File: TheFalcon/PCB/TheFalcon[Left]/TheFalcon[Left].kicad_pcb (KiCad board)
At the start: 2 copper layers, 173.3 x 142.5 mm, 171 parts, among them IC1 IS31FL3729-QFLS4-TR, J2 Conn_01x04_Pin, J3 Conn_01x04_Pin, J5 Conn_01x01, J6 Conn_01x01, SW1 SW_Push, SW2 SW_Push, U2 USBLC6-2P6, U3 USBLC6-2P6, U4 AMS1117-3.3, U6 STM32G431CBTx, Y1 X322516MOB4SI

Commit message: Save
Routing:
- net /RGB Array/R_RGB_ROW_2: track 143.3 -> 133.7 mm, vias 12 -> 0
- net /RGB Array/R_RGB_ROW_1: track 143.6 -> 134.4 mm, vias 12 -> 0
- net /RGB Array/R_RGB_ROW_0: track 148.1 -> 139.5 mm, vias 12 -> 0
- net /RGB Array/R_RGB_ROW_4: track 124.9 -> 117.0 mm, vias 10 -> 0
- net /RGB Array/R_RGB_ROW_3: track 140.8 -> 133.1 mm, vias 10 -> 0
- net +5V: track 141.1 -> 138.5 mm, vias 2 -> 0
- net /RGB Array/G_RGB_ROW_3: track 152.0 -> 150.5 mm, vias 2 -> 0
- added copper zone on In2.Cu, net GND
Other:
- copper layers 2 -> 4

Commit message: Save
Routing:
- net /RGB Array/G_RGB_ROW_0: track 162.3 -> 0.00 mm
- net /RGB Array/G_RGB_ROW_1: track 159.8 -> 1.56 mm
- net Row3: track 152.5 -> 0.00 mm
- net /RGB Array/B_RGB_ROW_2: track 152.2 -> 0.00 mm
- net /RGB Array/G_RGB_ROW_2: track 156.1 -> 6.92 mm
- net /RGB Array/B_RGB_ROW_1: track 148.9 -> 0.00 mm
- net /RGB Array/B_RGB_ROW_0: track 148.2 -> 0.00 mm
- net /RGB Array/B_RGB_ROW_3: track 145.5 -> 0.00 mm
- net Row1: track 136.7 -> 0.00 mm
- net Row2: track 136.4 -> 0.00 mm
- net /RGB Array/G_RGB_ROW_3: track 150.5 -> 15.6 mm
- net Row0: track 130.3 -> 0.00 mm
- net /RGB Array/G_RGB_ROW_4: track 133.3 -> 5.19 mm
- net /RGB Array/B_RGB_ROW_4: track 127.8 -> 0.00 mm
- net /RGB Array/R_RGB_ROW_3: track 133.1 -> 6.27 mm
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- added copper zone on In1.Cu, net GND
- removed copper zone on F.Cu, net GND

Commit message: Save
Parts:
- S1, S10, S11, S12, S13, S14, S15, S16, S17, S18, S19, S2, S20, S21, S22, S23, S24, S25, S26, S27, S28, S29, S3, S30, S31, S32, S33, S34, S4, S5, S6, S7, S8, S9: footprint Gateron_KS33_Hotswap:Gateron-KS33-Hotswap-1U_Model -> MX_KS33:MX_KS33-Solderable-1U; moved to F.Cu
- S35, S36: footprint Gateron_KS33_Hotswap:Gateron-KS33-Hotswap-1.5U -> MX_KS33:MX_KS33-Solderable-1.5U; moved to F.Cu

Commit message: Save
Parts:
- moved C9 129.4 mm to (129.5, 20.9), turned to 0 degrees
- moved SW1 128.6 mm to (133.9, 20.7), turned to 180 degrees
- moved R24 114.2 mm to (99.3, 129.1)
- moved R33 114.0 mm to (97.5, 127.1)
- moved C12 110.7 mm to (85.6, 126.1)
- moved IC1 110.7 mm to (84.0, 129.3)
- moved C13 110.7 mm to (85.6, 124.6)
- moved R6 110.7 mm to (87.6, 126.8)
- moved R4 109.8 mm to (150.4, 21.1)
- moved SW2 109.2 mm to (139.7, 20.7), turned to 180 degrees
- moved R3 107.0 mm to (145.8, 21.5)
- moved C1 102.5 mm to (113.3, 31.5), turned to -90 degrees
- moved C14 100.3 mm to (94.7, 130.1), turned to -90 degrees
- moved R5 99.7 mm to (92.9, 130.5), turned to -90 degrees
- moved C2 99.0 mm to (123.6, 29.2), turned to 180 degrees
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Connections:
- U6 pad 10: unconnected-(U6-PA2-Pad10) -> Row0
- U6 pad 11: unconnected-(U6-PA3-Pad11) -> Row1
- U6 pad 12: Row4 -> unconnected-(U6-PA4-Pad12)
- U6 pad 14: Col4 -> Row4
- U6 pad 15: Col3 -> unconnected-(U6-PA7-Pad15)
- U6 pad 16: Col2 -> unconnected-(U6-PB0-Pad16)
- U6 pad 17: Col1 -> unconnected-(U6-PB1-Pad17)
- U6 pad 18: Col0 -> unconnected-(U6-PB2-Pad18)
- U6 pad 22: Col6 -> unconnected-(U6-PB10-Pad22)
- U6 pad 25: Row3 -> unconnected-(U6-PB11-Pad25)
- U6 pad 26: Row2 -> Col4
- U6 pad 27: Row1 -> Col3
- U6 pad 28: Row0 -> Col2
- U6 pad 29: LED_MCU_SDB -> Col1
- U6 pad 3: unconnected-(U6-PC14-Pad3) -> Row3
- U6 pad 32: unconnected-(U6-PA10-Pad32) -> Col0
- U6 pad 4: unconnected-(U6-PC15-Pad4) -> Row2
- U6 pad 8: unconnected-(U6-PA0-Pad8) -> Col6
- U6 pad 9: unconnected-(U6-PA1-Pad9) -> LED_MCU_SDB
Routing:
- net Row3: track 0.00 -> 237.7 mm, vias 0 -> 7
- net Row2: track 0.00 -> 214.3 mm, vias 0 -> 7
- net Row0: track 0.00 -> 194.8 mm, vias 0 -> 7
- net /RGB Array/B_RGB_ROW_4: track 0.00 -> 193.6 mm, vias 0 -> 8
- net /RGB Array/G_RGB_ROW_4: track 5.19 -> 196.6 mm, vias 0 -> 8
- net /RGB Array/R_RGB_ROW_4: track 8.74 -> 195.8 mm, vias 0 -> 8
- net Col0: track 0.00 -> 178.3 mm, vias 0 -> 1
- net ThumbRow: track 0.00 -> 177.7 mm, vias 0 -> 3
- net /RGB Array/G_RGB_ROW_2: track 6.92 -> 181.0 mm, vias 0 -> 7
- net /RGB Array/G_RGB_ROW_0: track 0.00 -> 172.9 mm, vias 0 -> 7
- net Row1: track 0.00 -> 170.0 mm, vias 0 -> 7
- net /RGB Array/G_RGB_ROW_1: track 1.56 -> 168.3 mm, vias 0 -> 6
- net Col1: track 0.00 -> 163.9 mm, vias 0 -> 2
- net LED_MCU_SDB: track 0.00 -> 156.1 mm, vias 0 -> 4
- net /RGB Array/G_RGB_ROW_3: track 15.6 -> 167.7 mm, vias 0 -> 7
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- added copper zone on F.Cu, net +5V
- added copper zone on F.Cu, net VBUS

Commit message: Cleaning up
I have all connections, just cleaning up
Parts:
- added J1: Conn_01x01, Connector_Wire:SolderWire-0.1sqmm_1x01_D0.4mm_OD1mm, F.Cu at (136.6, 48.2)
- added J4: Conn_01x01, Connector_Wire:SolderWire-0.1sqmm_1x01_D0.4mm_OD1mm, F.Cu at (136.8, 85.2)
- added J7: Conn_01x01, Connector_Wire:SolderWire-0.1sqmm_1x01_D0.4mm_OD1mm, F.Cu at (141.2, 44.9)
- J3: value Conn_01x04_Pin -> Conn_01x01; footprint Connector_Wire:SolderWire-1sqmm_1x04_P5.4mm_D1.4mm_OD2.7mm -> Connector_Wire:SolderWire-0.1sqmm_1x01_D0.4mm_OD1mm; moved to F.Cu
- moved H4 218.3 mm to (162.5, 138.4)
- moved H1 208.9 mm to (141.2, 132.2)
- moved H5 121.2 mm to (80.3, 79.8)
- moved H3 118.3 mm to (137.2, 65.0)
- moved J3 116.3 mm to (111.2, 29.2), turned to 0 degrees
- moved H2 107.9 mm to (42.3, 104.8)
- moved J6 94.1 mm to (82.8, 40.6)
- moved J5 93.7 mm to (82.9, 37.8)
- moved R24 89.4 mm to (100.5, 39.8), turned to 180 degrees
- moved R33 85.9 mm to (102.1, 41.4), turned to 0 degrees
- moved H6 55.7 mm to (23.2, 44.9)
- moved R15 45.9 mm to (82.6, 88.5), turned to -90 degrees
- moved R16 42.2 mm to (79.2, 88.2), turned to 0 degrees
- moved R17 41.8 mm to (69.4, 89.9), turned to 0 degrees
- moved J2 26.6 mm to (167.0, 125.3), turned to -30 degrees
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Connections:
- J3 pad 1: PA15 -> PB4
- R15 pad 2: /RGB Array/CS8 -> /RGB Array/CS14
- R16 pad 2: /RGB Array/CS9 -> /RGB Array/CS15
- R17 pad 2: /RGB Array/CS7 -> /RGB Array/CS13
- R21 pad 2: /RGB Array/CS14 -> /RGB Array/CS8
- R22 pad 2: /RGB Array/CS15 -> /RGB Array/CS9
- R23 pad 2: /RGB Array/CS13 -> /RGB Array/CS7
- U6 pad 16: unconnected-(U6-PB0-Pad16) -> PB9
- U6 pad 42: PB5 -> unconnected-(U6-PB5-Pad42)
- U6 pad 46: PB9 -> unconnected-(U6-PB9-Pad46)
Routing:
- net NRST: track 0.00 -> 149.8 mm, vias 0 -> 2
- net SYS_JTAG_TRACE: track 0.00 -> 146.8 mm, vias 0 -> 1
- net SYS_JTAG_SWCLK: track 0.00 -> 144.4 mm, vias 0 -> 2
- net SYS_JTAG_SWDIO: track 0.00 -> 136.8 mm, vias 0 -> 1
- net +3.3V: track 87.3 -> 213.3 mm, vias 0 -> 10
- net /RGB Array/SW2: track 109.4 -> 194.4 mm, vias 8 -> 10
- net /RGB Array/CS10: track 0.00 -> 78.0 mm
- net /RGB Array/SW8: track 99.3 -> 174.7 mm, vias 5 -> 7
- net /RGB Array/CS11: track 5.62 -> 62.0 mm, vias 0 -> 2
- net /RGB Array/CS12: track 0.00 -> 55.3 mm
- net /RGB Array/CS7: track 0.00 -> 52.1 mm
- net /RGB Array/SW7: track 97.3 -> 146.5 mm, vias 8 -> 10
- net /RGB Array/CS13: track 0.00 -> 45.9 mm
- net /RGB Array/CS15: track 0.00 -> 42.4 mm, vias 0 -> 2
- net /RGB Array/CS14: track 0.00 -> 41.4 mm
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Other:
- board text added: "USB to PC"

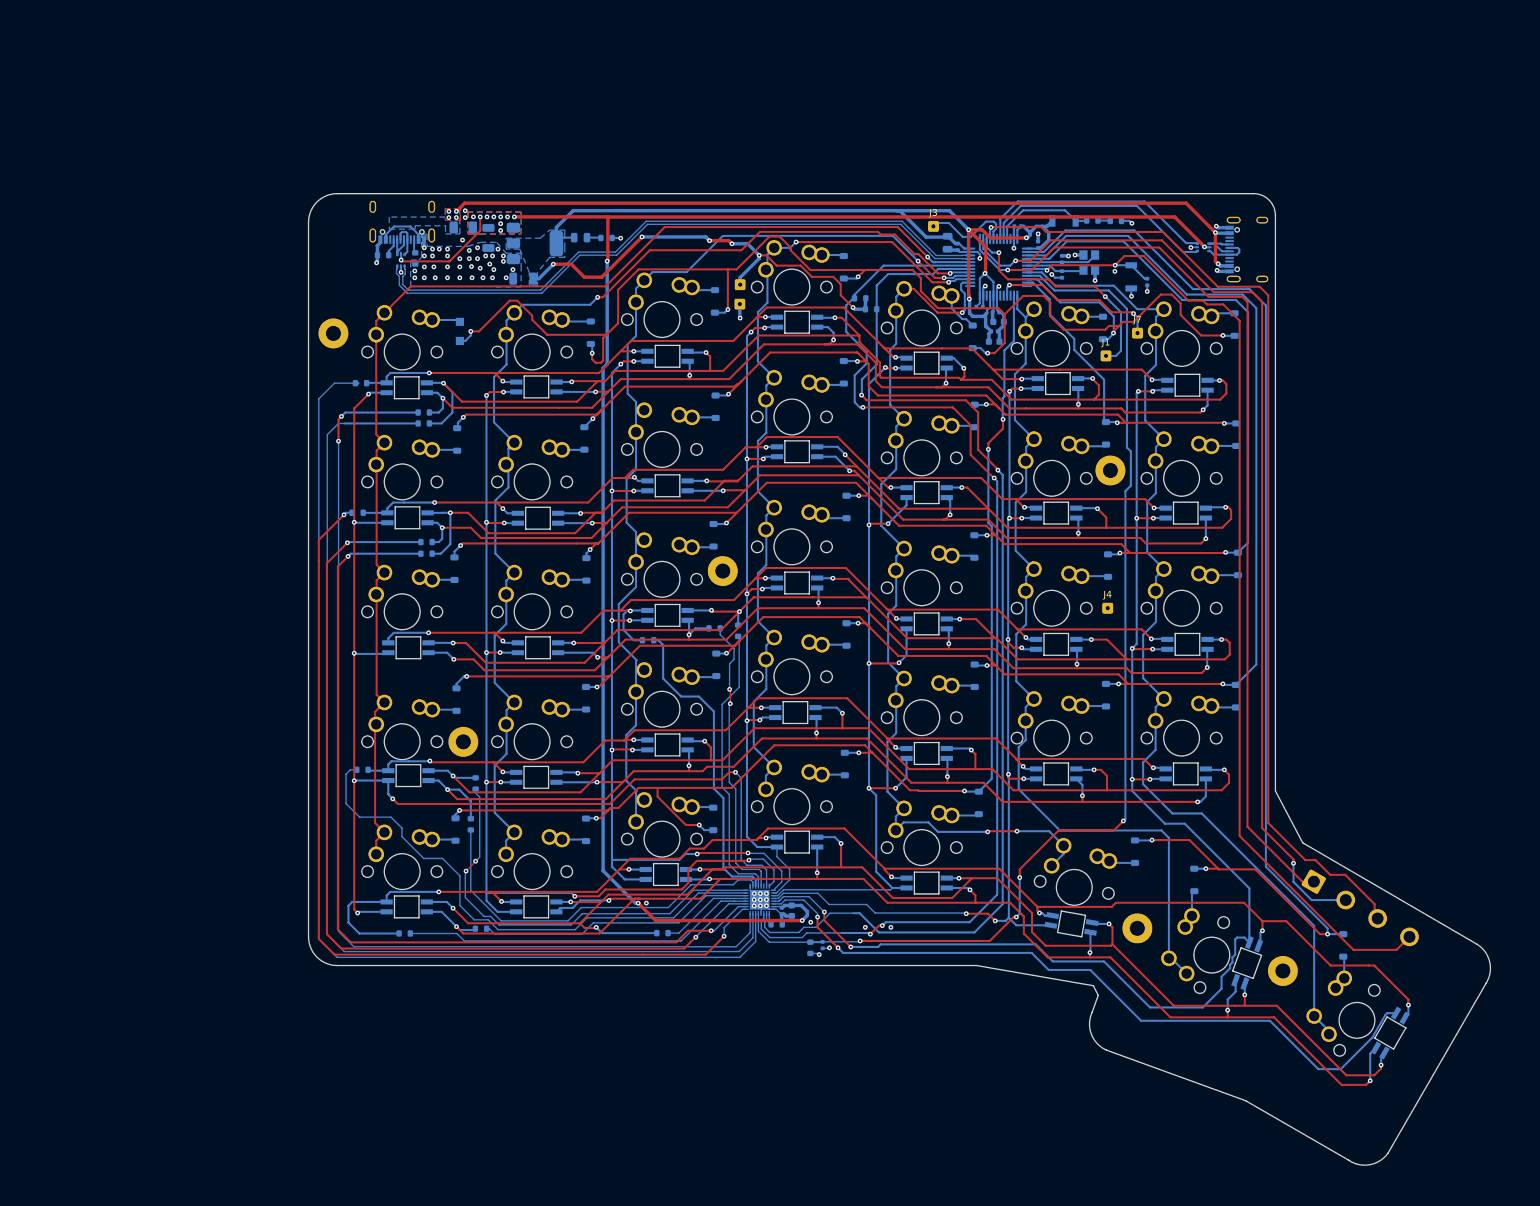
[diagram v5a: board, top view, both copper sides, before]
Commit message: Save
Done left side, going to start right side now
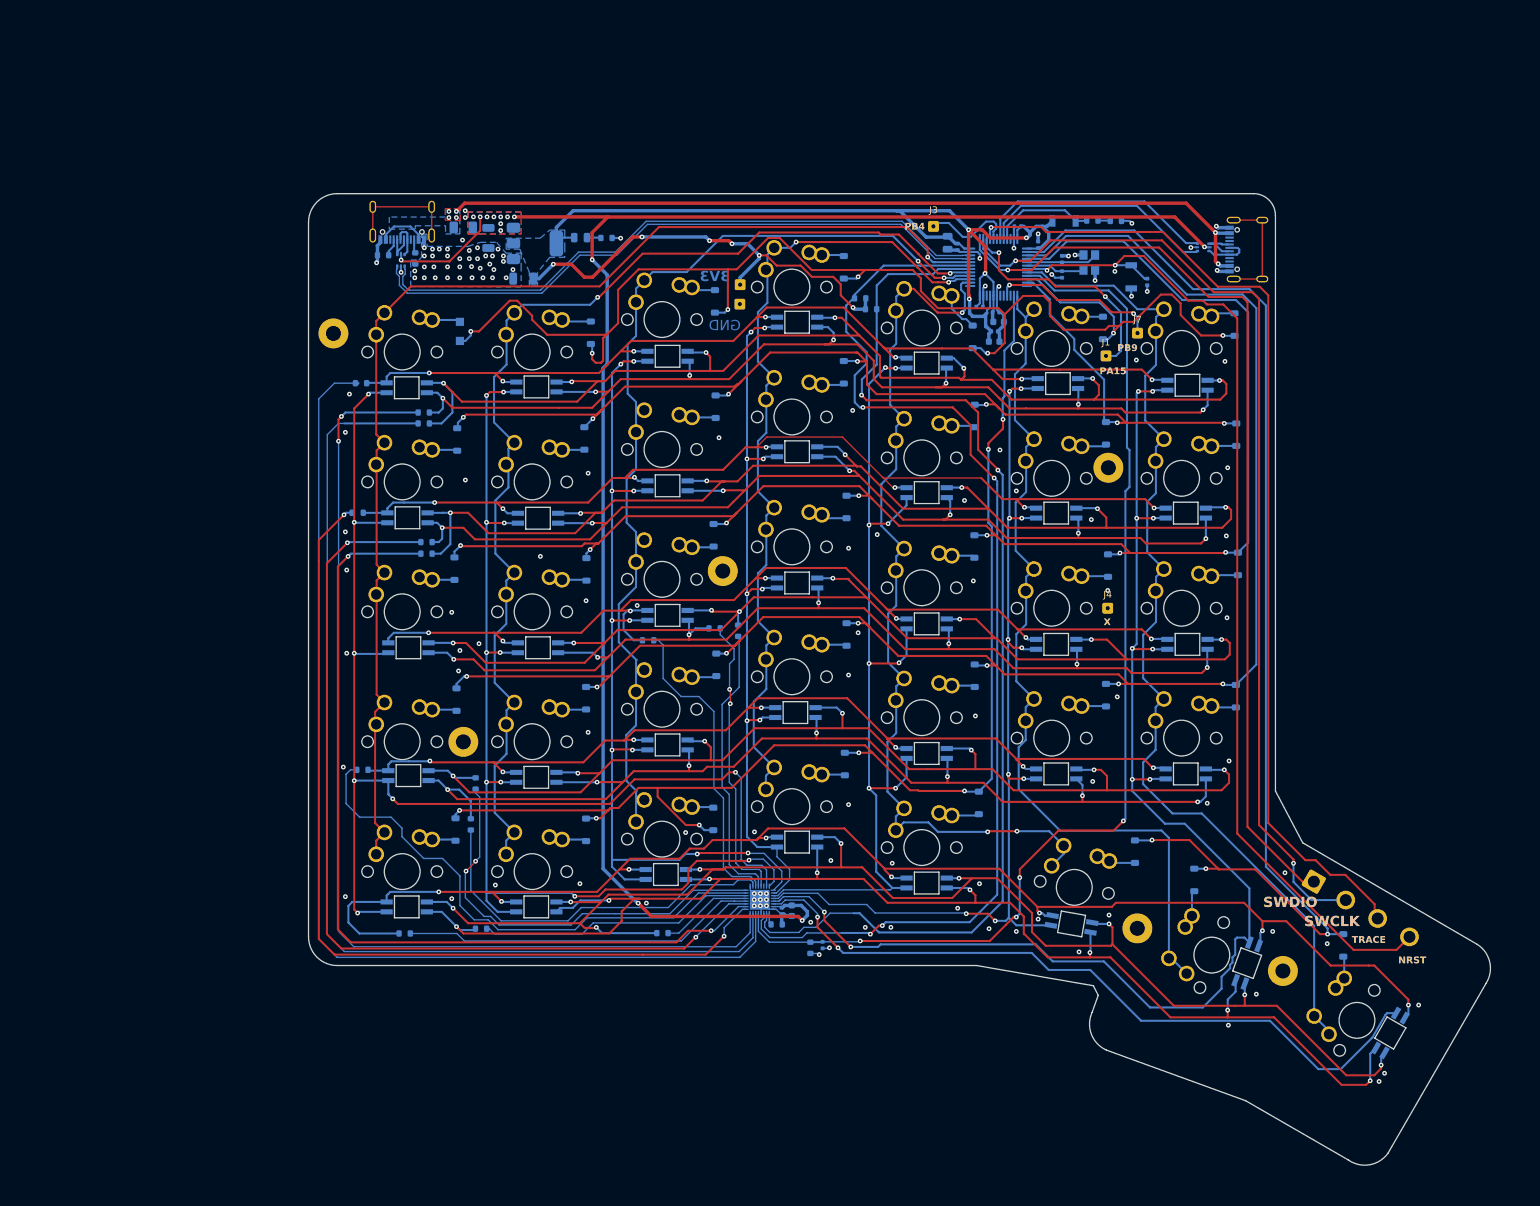
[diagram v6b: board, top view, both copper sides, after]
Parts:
- moved H3 0.50 mm to (136.9, 64.6)
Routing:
- net unconnected-(USB1-SHIELD-PadS1): track 0.00 -> 17.0 mm
- net unconnected-(USB2-SHIELD-PadS1): track 0.00 -> 17.0 mm
- net GND: track 60.3 -> 58.2 mm, vias 74 -> 135
- net /RGB Array/G_RGB_ROW_1: track 175.3 -> 173.3 mm
- net +5V: track 256.0 -> 257.6 mm
- net /RGB Array/R_RGB_ROW_4: track 204.5 -> 205.3 mm
- net Col0: track 178.3 -> 179.1 mm
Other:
- board text added: "3V3"
- board text added: "BOOT"
- board text added: "GND"
- board text added: "NRST"
- board text added: "PA15"
- board text added: "PB4"
- board text added: "PB9"
- board text added: "PWR LED"
- board text added: "SWCLK"
- board text added: "SWDIO"
- board text added: "TRACE"
- board text added: "USB SERIAL"
- board text added: "X"
